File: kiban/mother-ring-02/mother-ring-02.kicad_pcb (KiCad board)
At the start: 2 copper layers, 88 x 88 mm, 26 parts, among them J1 LED01, J10 CHARGE, J11 POWER, J12 5V, J13 3V3, J14 BATTERY, J15 POWER, J2 LED02, J3 LED03, J4 LED04, J5 LED05, J6 POWER-01, J7 POWER-02, J8 ESP32-01, J9 ESP32-01

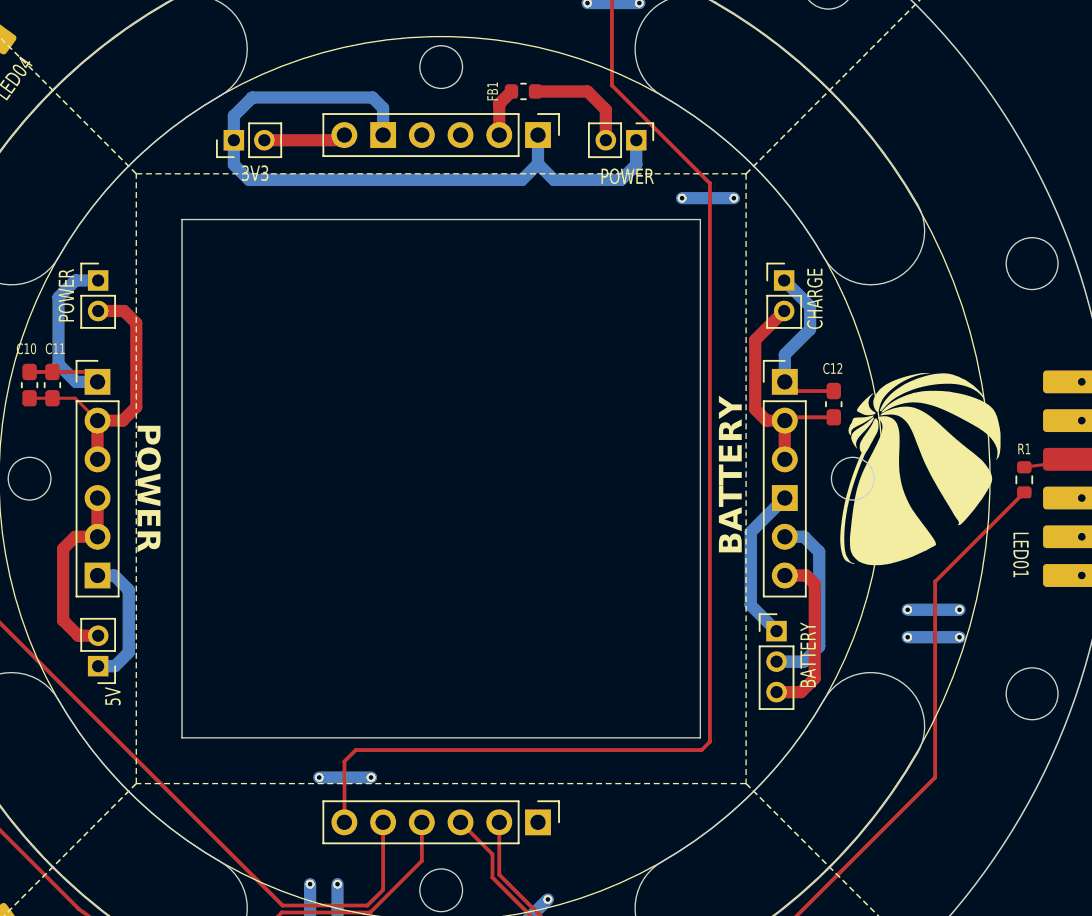
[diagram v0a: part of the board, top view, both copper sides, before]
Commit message: kiban: mother-ring board update + v02/v03 iterations
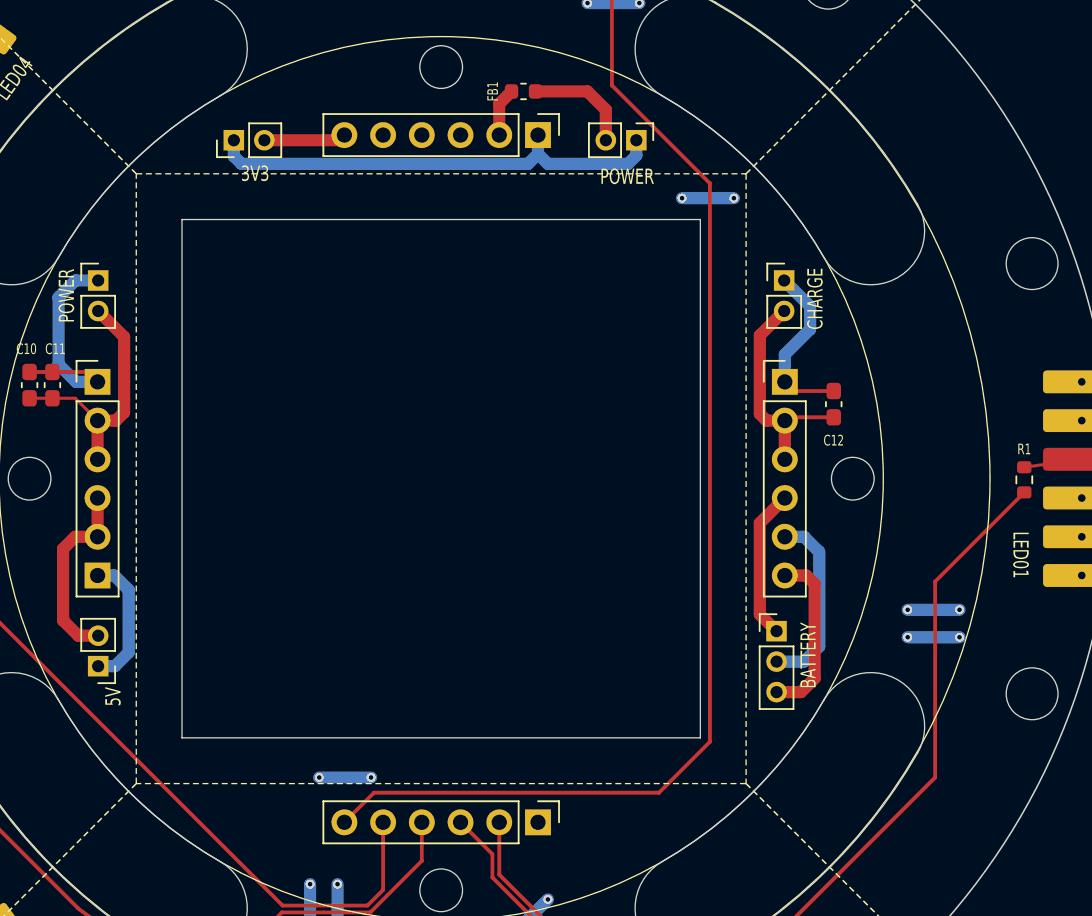
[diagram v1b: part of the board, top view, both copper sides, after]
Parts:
- removed G*** (x2): LOGO, LOGO
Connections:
- J14 pad 1: GND -> P+
- J14 pad 3: P+ -> P-
- J7 pad 4: GND -> P+
- J7 pad 6: P+ -> P-
- J8 pad 5: GND -> GPIO08
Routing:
- net GND: track 93.1 -> 66.3 mm
- net P-: track 0.00 -> 11.3 mm
- net GPIO05: track 85.0 -> 82.6 mm
- net +5V: track 72.4 -> 70.5 mm
- net P+: track 11.3 -> 9.86 mm
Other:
- board text removed: "BATTERY"
- board text removed: "ESP32"
- board text removed: "LED"
- board text removed: "POWER"
